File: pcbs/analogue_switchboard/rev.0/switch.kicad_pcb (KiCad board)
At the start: 2 copper layers, 68.6 x 31.8 mm, 92 parts, among them J1 Conn_01x11, J2 Conn_01x11, Q1 BSS84, Q10 BSS84, Q11 2N7002, Q12 2N7002, Q13 BSS84, Q14 2N7002, Q15 BSS84, Q16 BSS84, Q17 2N7002, Q18 2N7002, Q19 BSS84, Q2 2N7002, Q20 2N7002, Q21 BSS84, Q22 BSS84, Q23 2N7002, Q24 2N7002, Q25 BSS84, Q26 2N7002, Q27 BSS84, Q28 BSS84, Q29 2N7002, Q3 BSS84, Q30 2N7002, Q31 BSS84, Q32 2N7002, Q33 BSS84, Q34 BSS84, Q35 2N7002, Q36 2N7002, Q37 BSS84, Q38 2N7002, Q39 BSS84, Q4 BSS84, Q40 BSS84, Q41 2N7002, Q42 2N7002, Q43 BSS84, Q44 2N7002, Q45 BSS84, Q46 BSS84, Q47 2N7002, Q48 2N7002, Q49 BSS84, Q5 2N7002, Q50 2N7002, Q51 BSS84, Q52 BSS84, Q53 2N7002, Q54 2N7002, Q6 2N7002, Q7 BSS84, Q8 2N7002, Q9 BSS84

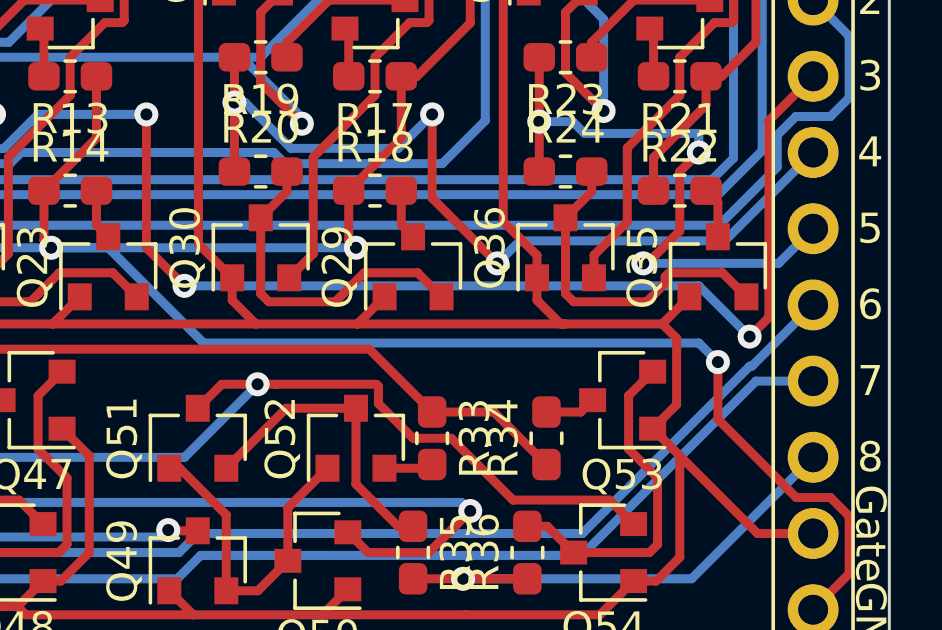
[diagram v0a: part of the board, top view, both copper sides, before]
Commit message: re-organized project directory and started work on ALU pcb
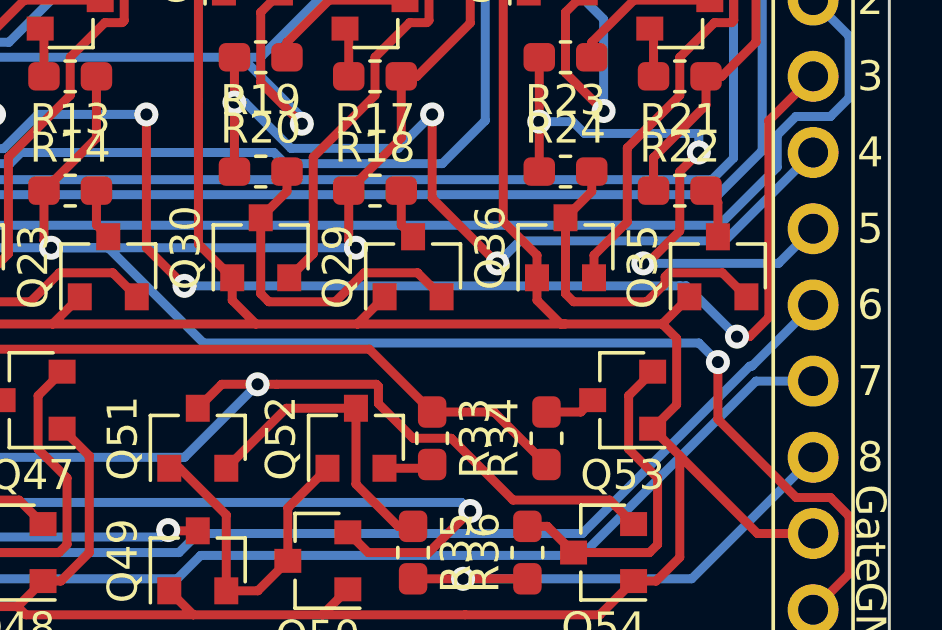
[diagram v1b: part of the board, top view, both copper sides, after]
